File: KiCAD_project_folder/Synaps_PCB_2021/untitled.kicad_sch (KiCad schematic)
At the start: 3 parts

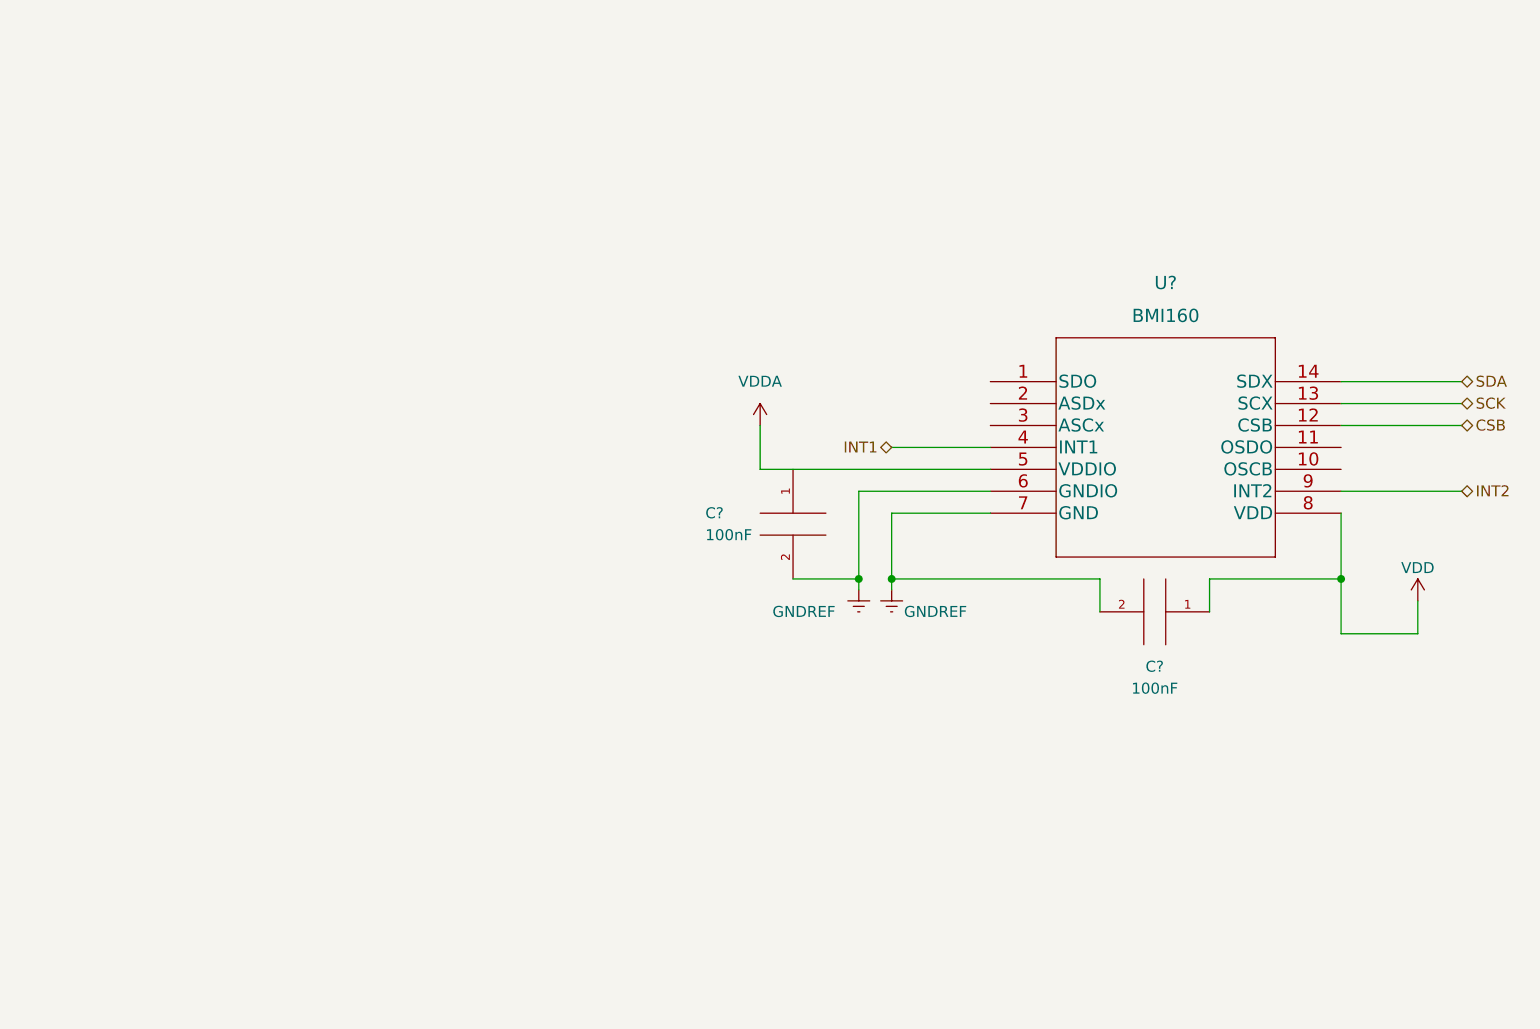
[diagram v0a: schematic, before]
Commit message: Added basic PCB guidelines
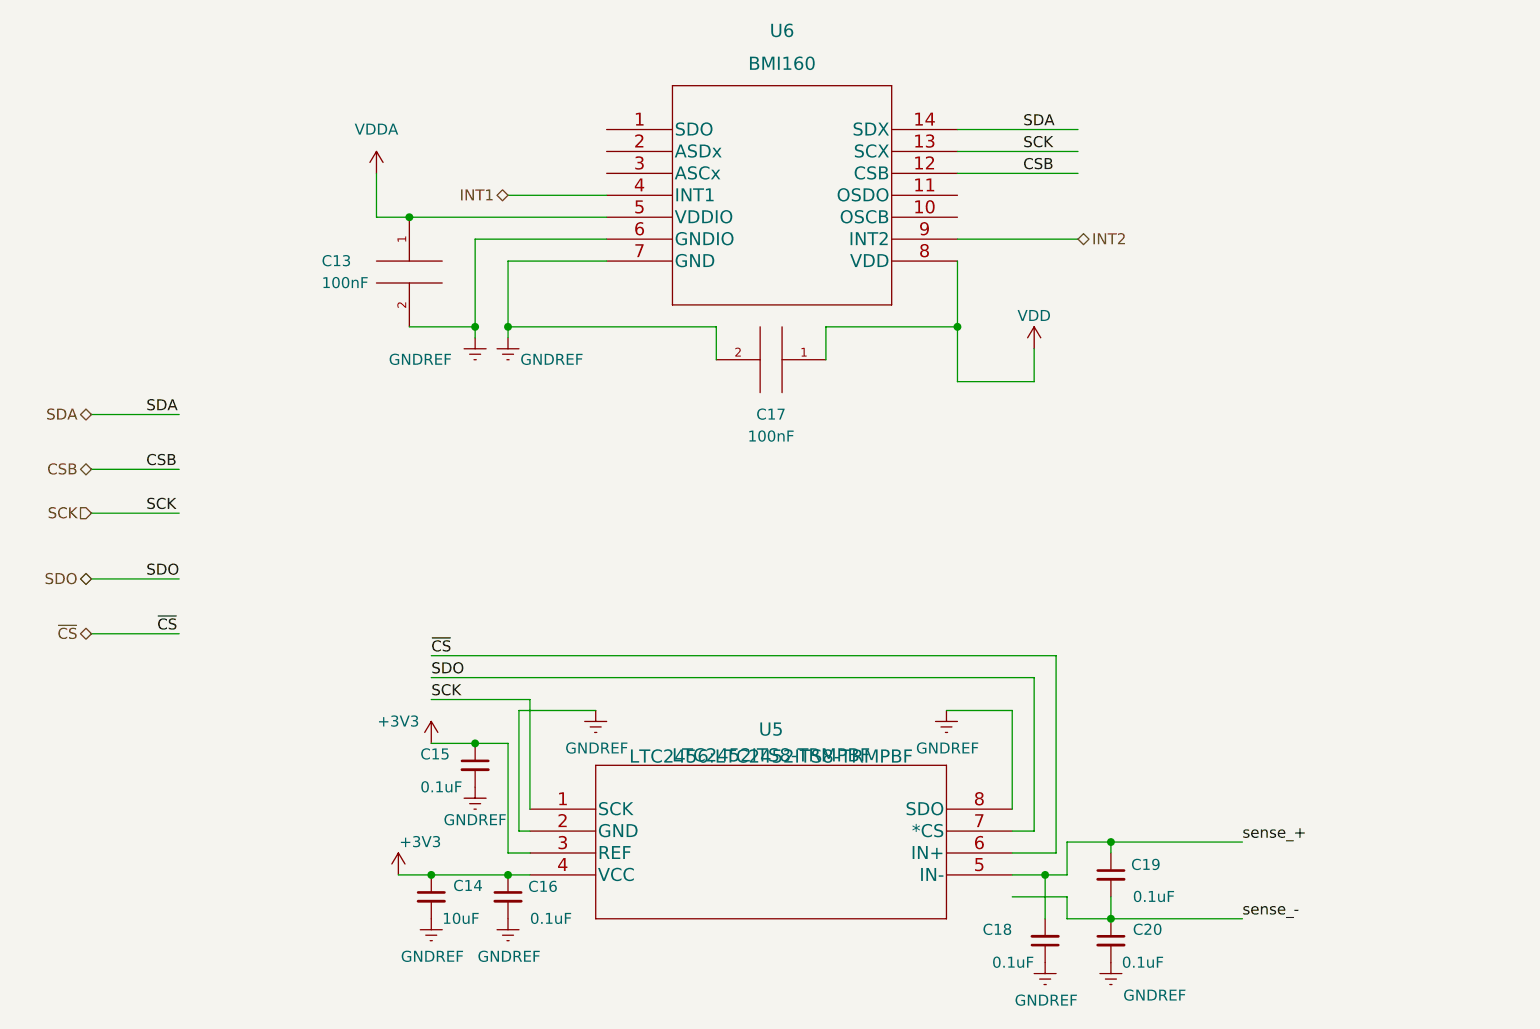
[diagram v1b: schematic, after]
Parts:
- added C14: 10uF, Capacitor_SMD:C_1206_3216Metric_Pad1.33x1.80mm_HandSolder, symbol Device:C_Small
- added C15, C16, C18, C19, C20: 0.1uF, Capacitor_SMD:C_1206_3216Metric_Pad1.33x1.80mm_HandSolder, symbol Device:C_Small
- added U5: LTC2452ITS8-TRMPBF, LTC2456:LTC2452ITS8-TRMPBF, symbol LTC2452:LTC2452ITS8-TRMPBF
- C13, C17: renamed from C?; footprint (none) -> Capacitor_SMD:C_1206_3216Metric_Pad1.33x1.80mm_HandSolder
- U6: renamed from U?; footprint LGA_BMI3X2P5_BOS -> BMI160:BMI160
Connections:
- net GNDREF: now also C14.2, C15.2, C16.2, C18.1, C20.2, U5.2 (GND), U5.8 (SDO)
- net SCK: now also U5.1 (SCK)
- net VDDA: now also C13.1
- new net +3V3: C14.1, C15.1, C16.1, U5.3 (REF), U5.4 (VCC)
- new net SDO: U5.7 (*CS)
- new net sense_+: C18.2, C19.1, U5.5 (IN-)
- new net sense_-: C19.2, C20.1
- new net ~{CS}: U5.6 (IN+)
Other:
- moved on the sheet: C13, C17, U6

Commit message: modified the battery file
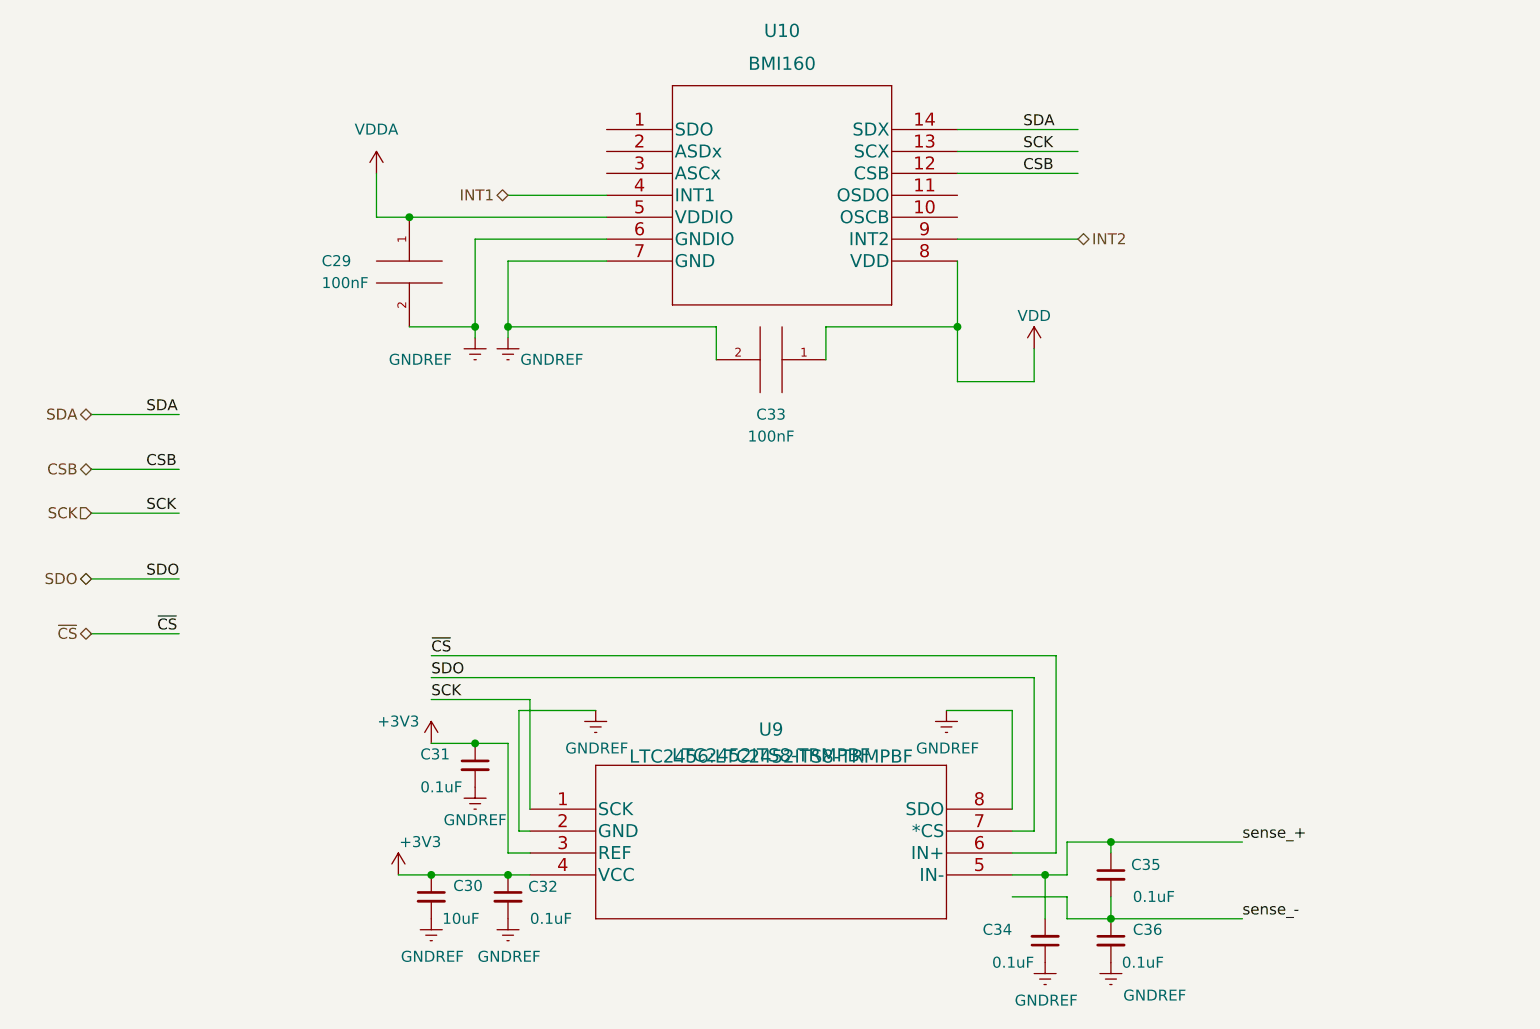
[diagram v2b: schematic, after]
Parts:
- renumbered C13 to C29, C14 to C30, C15 to C31, C16 to C32, C17 to C33, C18 to C34, C19 to C35, C20 to C36, U6 to U10, U5 to U9
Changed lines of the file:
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@@
   (symbol (lib_id "Device:C_Small") (at 156.21 123.19 0)
     (in_bom yes) (on_board yes)
-    (property "Reference" "C20" (id 0) (at 158.75 121.92 0)
+    (property "Reference" "C36" (id 0) (at 158.75 121.92 0)
       (effects (font (size 1.27 1.27)) (justify left))
     )
@@
   (symbol (lib_id "power:VDDA") (at 71.12 34.29 0)
     (in_bom yes) (on_board yes) (fields_autoplaced)
-    (property "Reference" "#PWR022" (id 0) (at 71.12 38.1 0)
+    (property "Reference" "#PWR048" (id 0) (at 71.12 38.1 0)
       (effects (font (size 1.27 1.27)) hide)
     )
@@
   (symbol (lib_id "Device:C_Small") (at 77.47 118.11 0)
     (in_bom yes) (on_board yes)
-    (property "Reference" "C14" (id 0) (at 80.01 116.84 0)
+    (property "Reference" "C30" (id 0) (at 80.01 116.84 0)
       (effects (font (size 1.27 1.27)) (justify left))
     )
@@
   (symbol (lib_id "power:GNDREF") (at 137.16 96.52 0)
     (in_bom yes) (on_board yes)
-    (property "Reference" "#PWR031" (id 0) (at 137.16 102.87 0)
+    (property "Reference" "#PWR057" (id 0) (at 137.16 102.87 0)
       (effects (font (size 1.27 1.27)) hide)
     )
@@
   (symbol (lib_id "power:GNDREF") (at 148.59 125.73 0)
     (in_bom yes) (on_board yes)
-    (property "Reference" "#PWR033" (id 0) (at 148.59 132.08 0)
+    (property "Reference" "#PWR059" (id 0) (at 148.59 132.08 0)
       (effects (font (size 1.27 1.27)) hide)
     )
@@
   (symbol (lib_id "Device:C_Small") (at 148.59 123.19 180)
     (in_bom yes) (on_board yes)
-    (property "Reference" "C18" (id 0) (at 144.78 121.92 0)
+    (property "Reference" "C34" (id 0) (at 144.78 121.92 0)
       (effects (font (size 1.27 1.27)) (justify left))
     )
@@
   (symbol (lib_id "pspice:CAP") (at 116.84 55.88 270)
     (in_bom yes) (on_board yes)
-    (property "Reference" "C17" (id 0) (at 116.84 62.23 90))
+    (property "Reference" "C33" (id 0) (at 116.84 62.23 90))
     (property "Value" "100nF" (id 1) (at 116.84 64.77 90))
     (property "Footprint" "Capacitor_SMD:C_1206_3216Metric_Pad1.33x1.80mm_HandSolder" (id 2) (at 116.84 55.88 0)
@@
   (symbol (lib_id "power:VDD") (at 147.32 54.61 0)
     (in_bom yes) (on_board yes)
-    (property "Reference" "#PWR032" (id 0) (at 147.32 58.42 0)
+    (property "Reference" "#PWR058" (id 0) (at 147.32 58.42 0)
       (effects (font (size 1.27 1.27)) hide)
     )
@@
   (symbol (lib_id "power:+3V3") (at 73.66 115.57 0)
     (in_bom yes) (on_board yes)
-    (property "Reference" "#PWR023" (id 0) (at 73.66 119.38 0)
+    (property "Reference" "#PWR049" (id 0) (at 73.66 119.38 0)
       (effects (font (size 1.27 1.27)) hide)
     )
@@
   (symbol (lib_id "Device:C_Small") (at 86.36 118.11 0)
     (in_bom yes) (on_board yes)
-    (property "Reference" "C16" (id 0) (at 88.6968 116.9416 0)
+    (property "Reference" "C32" (id 0) (at 88.6968 116.9416 0)
       (effects (font (size 1.27 1.27)) (justify left))
     )
@@
   (symbol (lib_id "Device:C_Small") (at 82.55 102.87 0)
     (in_bom yes) (on_board yes)
-    (property "Reference" "C15" (id 0) (at 76.2 101.6 0)
+    (property "Reference" "C31" (id 0) (at 76.2 101.6 0)
       (effects (font (size 1.27 1.27)) (justify left))
     )
@@
   (symbol (lib_id "power:GNDREF") (at 86.36 120.65 0)
     (in_bom yes) (on_board yes)
-    (property "Reference" "#PWR029" (id 0) (at 86.36 127 0)
+    (property "Reference" "#PWR055" (id 0) (at 86.36 127 0)
       (effects (font (size 1.27 1.27)) hide)
     )
@@
   (symbol (lib_id "power:GNDREF") (at 82.55 53.34 0)
     (in_bom yes) (on_board yes)
-    (property "Reference" "#PWR026" (id 0) (at 82.55 59.69 0)
+    (property "Reference" "#PWR052" (id 0) (at 82.55 59.69 0)
       (effects (font (size 1.27 1.27)) hide)
     )
@@
   (symbol (lib_id "power:GNDREF") (at 96.52 96.52 0)
     (in_bom yes) (on_board yes)
-    (property "Reference" "#PWR030" (id 0) (at 96.52 102.87 0)
+    (property "Reference" "#PWR056" (id 0) (at 96.52 102.87 0)
       (effects (font (size 1.27 1.27)) hide)
     )
@@
   (symbol (lib_id "power:GNDREF") (at 82.55 105.41 0)
     (in_bom yes) (on_board yes)
-    (property "Reference" "#PWR027" (id 0) (at 82.55 111.76 0)
+    (property "Reference" "#PWR053" (id 0) (at 82.55 111.76 0)
       (effects (font (size 1.27 1.27)) hide)
     )
@@
   (symbol (lib_id "power:+3V3") (at 77.47 100.33 0)
     (in_bom yes) (on_board yes)
-    (property "Reference" "#PWR024" (id 0) (at 77.47 104.14 0)
+    (property "Reference" "#PWR050" (id 0) (at 77.47 104.14 0)
       (effects (font (size 1.27 1.27)) hide)
     )
@@
   (symbol (lib_id "power:GNDREF") (at 77.47 120.65 0)
     (in_bom yes) (on_board yes)
-    (property "Reference" "#PWR025" (id 0) (at 77.47 127 0)
+    (property "Reference" "#PWR051" (id 0) (at 77.47 127 0)
       (effects (font (size 1.27 1.27)) hide)
     )
@@
   (symbol (lib_id "power:GNDREF") (at 86.36 53.34 0)
     (in_bom yes) (on_board yes)
-    (property "Reference" "#PWR028" (id 0) (at 86.36 59.69 0)
+    (property "Reference" "#PWR054" (id 0) (at 86.36 59.69 0)
       (effects (font (size 1.27 1.27)) hide)
     )
@@
   (symbol (lib_id "Device:C_Small") (at 156.21 115.57 0)
     (in_bom yes) (on_board yes)
-    (property "Reference" "C19" (id 0) (at 158.5468 114.4016 0)
+    (property "Reference" "C35" (id 0) (at 158.5468 114.4016 0)
       (effects (font (size 1.27 1.27)) (justify left))
     )
@@
   (symbol (lib_id "LTC2452:LTC2452ITS8-TRMPBF") (at 88.9 107.95 0)
     (in_bom yes) (on_board yes) (fields_autoplaced)
-    (property "Reference" "U5" (id 0) (at 116.84 98.7224 0)
+    (property "Reference" "U9" (id 0) (at 116.84 98.7224 0)
       (effects (font (size 1.524 1.524)))
     )
@@
   (symbol (lib_id "BM160:BMI160") (at 97.79 29.21 0)
     (in_bom yes) (on_board yes) (fields_autoplaced)
-    (property "Reference" "U6" (id 0) (at 118.11 17.78 0)
+    (property "Reference" "U10" (id 0) (at 118.11 17.78 0)
       (effects (font (size 1.524 1.524)))
     )
@@
   (symbol (lib_id "power:GNDREF") (at 156.21 125.73 0)
     (in_bom yes) (on_board yes)
-    (property "Reference" "#PWR034" (id 0) (at 156.21 132.08 0)
+    (property "Reference" "#PWR060" (id 0) (at 156.21 132.08 0)
       (effects (font (size 1.27 1.27)) hide)
     )
@@
   (symbol (lib_id "pspice:CAP") (at 74.93 45.72 0)
     (in_bom yes) (on_board yes)
-    (property "Reference" "C13" (id 0) (at 64.77 44.45 0)
-      (effects (font (size 1.27 1.27)) (justify left))
-    )
+    (property "Reference" "C29" (id 0) (at 64.77 44.45 0)
+      (effects (font (size 1.27 1.27)) (justify left))
+    )
